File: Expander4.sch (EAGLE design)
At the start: 6 parts, among them K1 G5L, K2 G5L, K3 G5L, K4 G5L

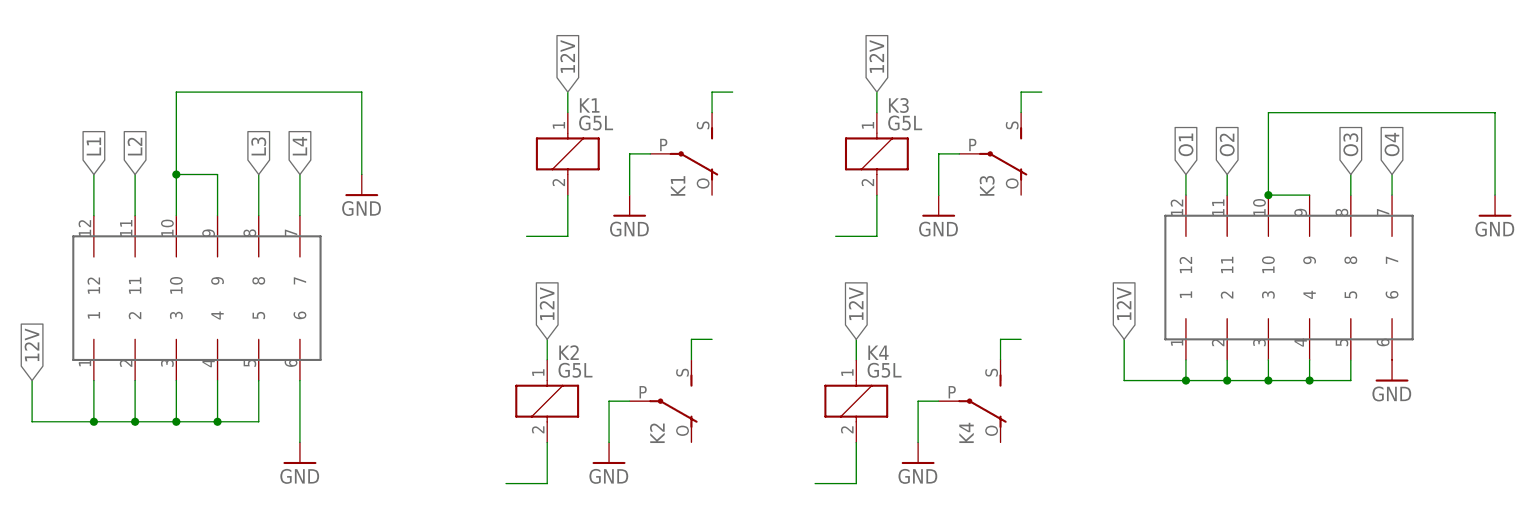
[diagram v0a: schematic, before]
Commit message: Protective diodes added in expander
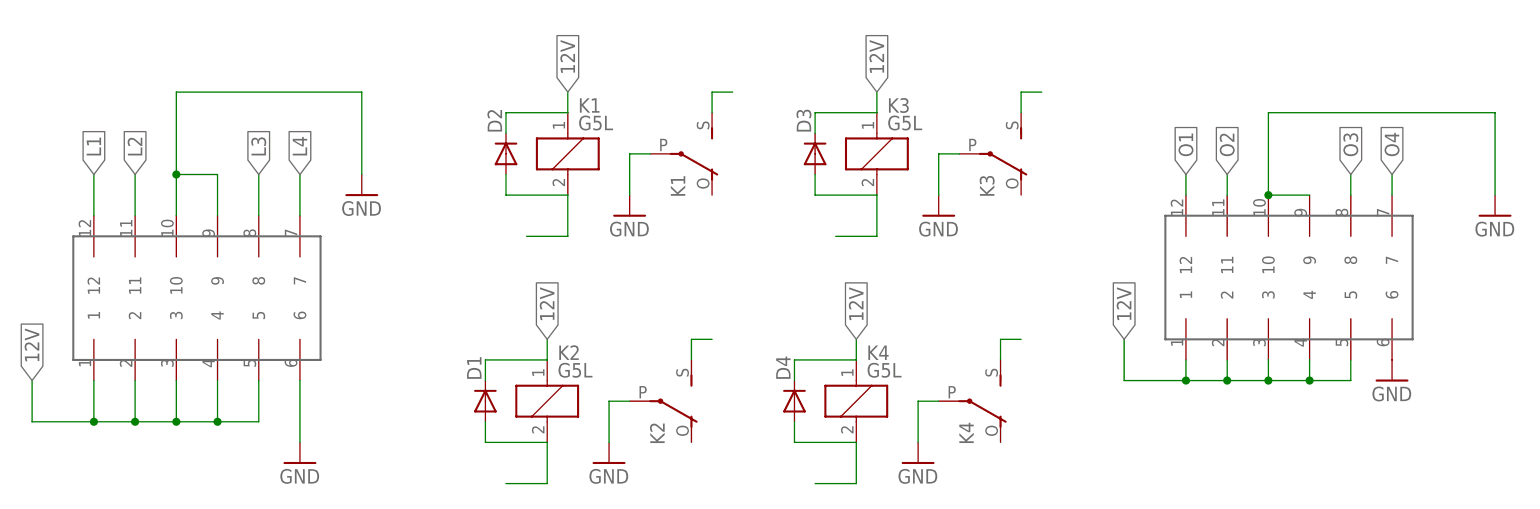
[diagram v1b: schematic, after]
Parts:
- added D1, D2, D3, D4: (no value), SparkFun-DiscreteSemi:DIODESMB
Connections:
- net 12V: now also D1.C, D2.C, D3.C, D4.C
- net L1: now also D2.A
- net L2: now also D1.A
- net L3: now also D3.A
- net L4: now also D4.A
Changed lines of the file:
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@@
 <part name="GND8" library="supply1" deviceset="GND" device=""/>
 <part name="GND7" library="supply1" deviceset="GND" device=""/>
+<part name="D1" library="SparkFun-DiscreteSemi" deviceset="DIODE" device="SMB"/>
+<part name="D2" library="SparkFun-DiscreteSemi" deviceset="DIODE" device="SMB"/>
+<part name="D3" library="SparkFun-DiscreteSemi" deviceset="DIODE" device="SMB"/>
+<part name="D4" library="SparkFun-DiscreteSemi" deviceset="DIODE" device="SMB"/>
 </parts>
 <sheets>
@@
 <instance part="GND8" gate="1" x="167.64" y="38.1"/>
 <instance part="GND7" gate="1" x="180.34" y="58.42"/>
+<instance part="D1" gate="G$1" x="55.88" y="35.56" rot="R90"/>
+<instance part="D2" gate="G$1" x="58.42" y="66.04" rot="R90"/>
+<instance part="D3" gate="G$1" x="96.52" y="66.04" rot="R90"/>
+<instance part="D4" gate="G$1" x="93.98" y="35.56" rot="R90"/>
 </instances>
 <busses>
@@
 <wire x1="66.04" y1="71.12" x2="66.04" y2="73.66" width="0.1524" layer="91"/>
 <label x="66.04" y="73.66" size="1.778" layer="95" rot="R90" xref="yes"/>
+<pinref part="D2" gate="G$1" pin="C"/>
+<wire x1="58.42" y1="68.58" x2="58.42" y2="71.12" width="0.1524" layer="91"/>
+<wire x1="58.42" y1="71.12" x2="66.04" y2="71.12" width="0.1524" layer="91"/>
 </segment>
 <segment>
@@
 <wire x1="63.5" y1="40.64" x2="63.5" y2="43.18" width="0.1524" layer="91"/>
 <label x="63.5" y="43.18" size="1.778" layer="95" rot="R90" xref="yes"/>
+<pinref part="D1" gate="G$1" pin="C"/>
+<wire x1="55.88" y1="38.1" x2="55.88" y2="40.64" width="0.1524" layer="91"/>
+<wire x1="55.88" y1="40.64" x2="63.5" y2="40.64" width="0.1524" layer="91"/>
 </segment>
 <segment>
@@
 <wire x1="104.14" y1="71.12" x2="104.14" y2="73.66" width="0.1524" layer="91"/>
 <label x="104.14" y="73.66" size="1.778" layer="95" rot="R90" xref="yes"/>
+<pinref part="D3" gate="G$1" pin="C"/>
+<wire x1="96.52" y1="68.58" x2="96.52" y2="71.12" width="0.1524" layer="91"/>
+<wire x1="96.52" y1="71.12" x2="104.14" y2="71.12" width="0.1524" layer="91"/>
 </segment>
 <segment>
@@
 <wire x1="101.6" y1="40.64" x2="101.6" y2="43.18" width="0.1524" layer="91"/>
 <label x="101.6" y="43.18" size="1.778" layer="95" rot="R90" xref="yes"/>
+<pinref part="D4" gate="G$1" pin="C"/>
+<wire x1="93.98" y1="38.1" x2="93.98" y2="40.64" width="0.1524" layer="91"/>
+<wire x1="93.98" y1="40.64" x2="101.6" y2="40.64" width="0.1524" layer="91"/>
 </segment>
 <segment>
@@
 <wire x1="66.04" y1="60.96" x2="66.04" y2="55.88" width="0.1524" layer="91"/>
 <wire x1="66.04" y1="55.88" x2="60.96" y2="55.88" width="0.1524" layer="91"/>
+<pinref part="D2" gate="G$1" pin="A"/>
+<wire x1="58.42" y1="63.5" x2="58.42" y2="60.96" width="0.1524" layer="91"/>
+<wire x1="58.42" y1="60.96" x2="66.04" y2="60.96" width="0.1524" layer="91"/>
 </segment>
 </net>
@@
 <wire x1="63.5" y1="30.48" x2="63.5" y2="25.4" width="0.1524" layer="91"/>
 <wire x1="63.5" y1="25.4" x2="58.42" y2="25.4" width="0.1524" layer="91"/>
+<pinref part="D1" gate="G$1" pin="A"/>
+<wire x1="55.88" y1="33.02" x2="55.88" y2="30.48" width="0.1524" layer="91"/>
+<wire x1="55.88" y1="30.48" x2="63.5" y2="30.48" width="0.1524" layer="91"/>
 </segment>
 </net>
@@
 <wire x1="104.14" y1="60.96" x2="104.14" y2="55.88" width="0.1524" layer="91"/>
 <wire x1="104.14" y1="55.88" x2="99.06" y2="55.88" width="0.1524" layer="91"/>
+<pinref part="D3" gate="G$1" pin="A"/>
+<wire x1="96.52" y1="63.5" x2="96.52" y2="60.96" width="0.1524" layer="91"/>
+<wire x1="96.52" y1="60.96" x2="104.14" y2="60.96" width="0.1524" layer="91"/>
 </segment>
 </net>
@@
 <wire x1="101.6" y1="30.48" x2="101.6" y2="25.4" width="0.1524" layer="91"/>
 <wire x1="101.6" y1="25.4" x2="96.52" y2="25.4" width="0.1524" layer="91"/>
-</segment>
-</net>
+<wire x1="93.98" y1="30.48" x2="101.6" y2="30.48" width="0.1524" layer="91"/>
+<pinref part="D4" gate="G$1" pin="A"/>
+<wire x1="93.98" y1="30.48" x2="93.98" y2="33.02" width="0.1524" layer="91"/>
+</segment>
+</net>
